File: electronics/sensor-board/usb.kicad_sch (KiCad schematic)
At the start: 6 parts, among them J16 USB_C_Receptacle_USB2.0

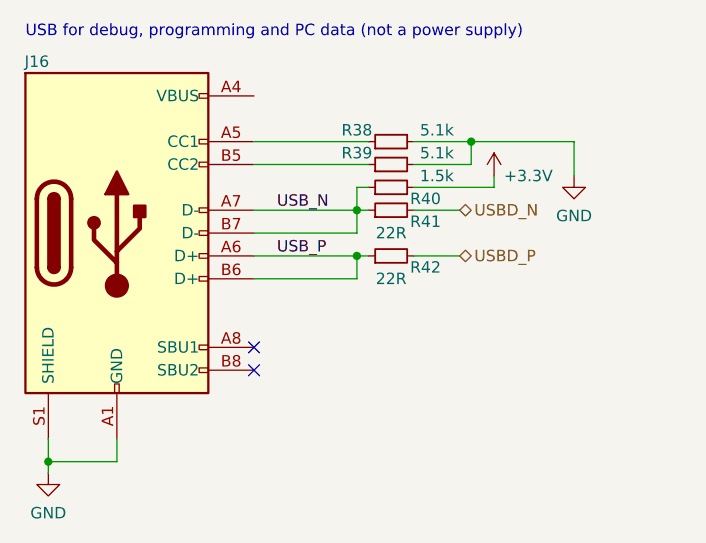
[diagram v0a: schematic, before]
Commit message: Upgrade to STM32G4 and CAN FD
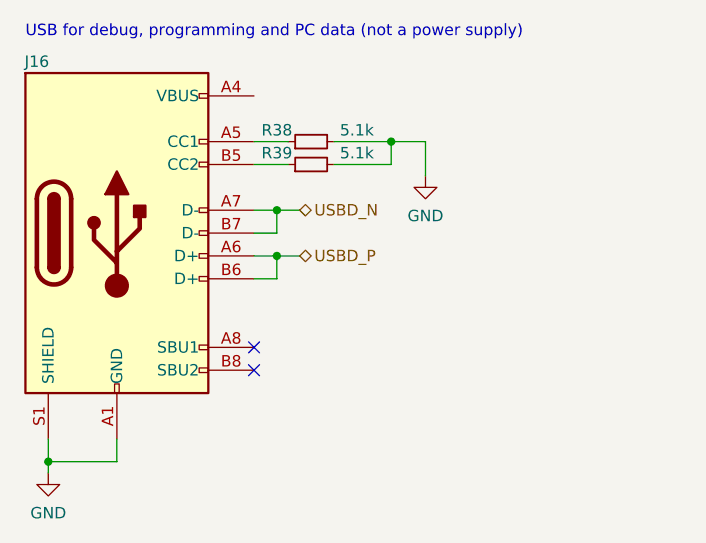
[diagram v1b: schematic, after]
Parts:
- removed R40: 1.5k, Resistor_SMD:R_0603_1608Metric, symbol Device:R_Small
- removed R41, R42: 22R, Resistor_SMD:R_0603_1608Metric, symbol Device:R_Small
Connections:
- net USB_N is gone; now on net USBD_N: J16.A7 (D-), J16.B7 (D-)
- net USB_P is gone; now on net USBD_P: J16.A6 (D+), J16.B6 (D+)
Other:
- moved on the sheet: R38, R39
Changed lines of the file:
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@@
 (kicad_sch (version 20211123) (generator eeschema)
   (paper "A4")
-  (junction (at 57.15 41.91) (diameter 0) (color 0 0 0 0)
+  (junction (at 48.26 41.91) (diameter 0) (color 0 0 0 0)
+  )
+  (junction (at 48.26 46.99) (diameter 0) (color 0 0 0 0)
   )
   (junction (at 22.86 69.85) (diameter 0) (color 0 0 0 0)
   )
-  (junction (at 69.85 34.29) (diameter 0) (color 0 0 0 0)
-  )
-  (junction (at 57.15 46.99) (diameter 0) (color 0 0 0 0)
+  (junction (at 60.96 34.29) (diameter 0) (color 0 0 0 0)
   )
   (no_connect (at 45.72 57.15))
@@
     (stroke (width 0) (type default) (color 0 0 0 0))
   )
-  (wire (pts (xy 69.85 34.29) (xy 81.28 34.29))
+  (wire (pts (xy 45.72 46.99) (xy 48.26 46.99))
     (stroke (width 0) (type default) (color 0 0 0 0))
   )
-  (wire (pts (xy 45.72 46.99) (xy 57.15 46.99))
+  (wire (pts (xy 45.72 36.83) (xy 49.53 36.83))
     (stroke (width 0) (type default) (color 0 0 0 0))
   )
-  (wire (pts (xy 45.72 36.83) (xy 58.42 36.83))
-    (stroke (width 0) (type default) (color 0 0 0 0))
-  )
-  (wire (pts (xy 45.72 41.91) (xy 57.15 41.91))
+  (wire (pts (xy 60.96 34.29) (xy 64.77 34.29))
     (stroke (width 0) (type default) (color 0 0 0 0))
   )
@@
     (stroke (width 0) (type default) (color 0 0 0 0))
   )
-  (wire (pts (xy 57.15 46.99) (xy 58.42 46.99))
-    (stroke (width 0) (type default) (color 0 0 0 0))
-  )
-  (wire (pts (xy 57.15 39.37) (xy 58.42 39.37))
-    (stroke (width 0) (type default) (color 0 0 0 0))
-  )
-  (wire (pts (xy 69.85 36.83) (xy 69.85 34.29))
+  (wire (pts (xy 60.96 36.83) (xy 60.96 34.29))
     (stroke (width 0) (type default) (color 0 0 0 0))
   )
@@
     (stroke (width 0) (type default) (color 0 0 0 0))
   )
-  (wire (pts (xy 63.5 39.37) (xy 72.39 39.37))
+  (wire (pts (xy 48.26 46.99) (xy 50.8 46.99))
     (stroke (width 0) (type default) (color 0 0 0 0))
   )
-  (wire (pts (xy 57.15 41.91) (xy 57.15 39.37))
+  (wire (pts (xy 48.26 41.91) (xy 50.8 41.91))
     (stroke (width 0) (type default) (color 0 0 0 0))
   )
-  (wire (pts (xy 57.15 41.91) (xy 58.42 41.91))
+  (wire (pts (xy 48.26 46.99) (xy 48.26 49.53))
     (stroke (width 0) (type default) (color 0 0 0 0))
   )
-  (wire (pts (xy 63.5 46.99) (xy 68.58 46.99))
+  (wire (pts (xy 45.72 34.29) (xy 49.53 34.29))
     (stroke (width 0) (type default) (color 0 0 0 0))
   )
-  (wire (pts (xy 57.15 46.99) (xy 57.15 49.53))
+  (wire (pts (xy 48.26 41.91) (xy 48.26 44.45))
     (stroke (width 0) (type default) (color 0 0 0 0))
   )
-  (wire (pts (xy 45.72 34.29) (xy 58.42 34.29))
-    (stroke (width 0) (type default) (color 0 0 0 0))
-  )
-  (wire (pts (xy 57.15 41.91) (xy 57.15 44.45))
-    (stroke (width 0) (type default) (color 0 0 0 0))
-  )
-  (wire (pts (xy 63.5 41.91) (xy 68.58 41.91))
+  (wire (pts (xy 45.72 41.91) (xy 48.26 41.91))
     (stroke (width 0) (type default) (color 0 0 0 0))
   )
@@
     (stroke (width 0) (type default) (color 0 0 0 0))
   )
-  (wire (pts (xy 69.85 34.29) (xy 63.5 34.29))
+  (wire (pts (xy 45.72 49.53) (xy 48.26 49.53))
     (stroke (width 0) (type default) (color 0 0 0 0))
   )
-  (wire (pts (xy 45.72 49.53) (xy 57.15 49.53))
+  (wire (pts (xy 54.61 36.83) (xy 60.96 36.83))
     (stroke (width 0) (type default) (color 0 0 0 0))
   )
-  (wire (pts (xy 63.5 36.83) (xy 69.85 36.83))
+  (wire (pts (xy 45.72 44.45) (xy 48.26 44.45))
     (stroke (width 0) (type default) (color 0 0 0 0))
   )
-  (wire (pts (xy 45.72 44.45) (xy 57.15 44.45))
+  (wire (pts (xy 64.77 34.29) (xy 64.77 38.1))
     (stroke (width 0) (type default) (color 0 0 0 0))
   )
-  (wire (pts (xy 81.28 34.29) (xy 81.28 38.1))
-    (stroke (width 0) (type default) (color 0 0 0 0))
-  )
-  (wire (pts (xy 72.39 39.37) (xy 72.39 38.1))
+  (wire (pts (xy 54.61 34.29) (xy 60.96 34.29))
     (stroke (width 0) (type default) (color 0 0 0 0))
   )
@@
     (effects (font (size 1.27 1.27)) (justify left bottom))
   )
-  (label "USB_P" (at 48.26 46.99 0)
-    (effects (font (size 1.27 1.27)) (justify left bottom))
-  )
-  (label "USB_N" (at 48.26 41.91 0)
-    (effects (font (size 1.27 1.27)) (justify left bottom))
-  )
-  (hierarchical_label "USBD_N" (shape bidirectional) (at 68.58 41.91 0)
+  (hierarchical_label "USBD_N" (shape bidirectional) (at 50.8 41.91 0)
     (effects (font (size 1.27 1.27)) (justify left))
   )
-  (hierarchical_label "USBD_P" (shape bidirectional) (at 68.58 46.99 0)
+  (hierarchical_label "USBD_P" (shape bidirectional) (at 50.8 46.99 0)
     (effects (font (size 1.27 1.27)) (justify left))
   )
-  (symbol (lib_id "power:GND") (at 81.28 38.1 0) (unit 1)
+  (symbol (lib_id "power:GND") (at 64.77 38.1 0) (unit 1)
     (in_bom yes) (on_board yes) (fields_autoplaced)
-    (property "Reference" "#PWR095" (id 0) (at 81.28 44.45 0)
+    (property "Reference" "#PWR095" (id 0) (at 64.77 44.45 0)
       (effects (font (size 1.27 1.27)) hide)
     )
-    (property "Value" "GND" (id 1) (at 81.28 42.5434 0))
-    (property "Footprint" "" (id 2) (at 81.28 38.1 0)
+    (property "Value" "GND" (id 1) (at 64.77 42.5434 0))
+    (property "Footprint" "" (id 2) (at 64.77 38.1 0)
       (effects (font (size 1.27 1.27)) hide)
     )
-    (property "Datasheet" "" (id 3) (at 81.28 38.1 0)
+    (property "Datasheet" "" (id 3) (at 64.77 38.1 0)
       (effects (font (size 1.27 1.27)) hide)
     )
     (pin "1")
   )
-  (symbol (lib_id "Device:R_Small") (at 60.96 39.37 90) (unit 1)
+  (symbol (lib_id "Device:R_Small") (at 52.07 36.83 90) (unit 1)
     (in_bom yes) (on_board yes)
-    (property "Reference" "R40" (id 0) (at 64.77 40.64 90))
-    (property "Value" "1.5k" (id 1) (at 66.04 38.1 90))
-    (property "Footprint" "Resistor_SMD:R_0603_1608Metric" (id 2) (at 60.96 39.37 0)
+    (property "Reference" "R39" (id 0) (at 48.26 35.56 90))
+    (property "Value" "5.1k" (id 1) (at 57.15 35.56 90))
+    (property "Footprint" "Resistor_SMD:R_0603_1608Metric" (id 2) (at 52.07 36.83 0)
       (effects (font (size 1.27 1.27)) hide)
     )
-    (property "Datasheet" "~" (id 3) (at 60.96 39.37 0)
+    (property "Datasheet" "~" (id 3) (at 52.07 36.83 0)
       (effects (font (size 1.27 1.27)) hide)
     )
     (pin "1")
     (pin "2")
-  )
-  (symbol (lib_id "Device:R_Small") (at 60.96 36.83 90) (unit 1)
-    (in_bom yes) (on_board yes)
-    (property "Reference" "R39" (id 0) (at 57.15 35.56 90))
-    (property "Value" "5.1k" (id 1) (at 66.04 35.56 90))
-    (property "Footprint" "Resistor_SMD:R_0603_1608Metric" (id 2) (at 60.96 36.83 0)
-      (effects (font (size 1.27 1.27)) hide)
-    )
-    (property "Datasheet" "~" (id 3) (at 60.96 36.83 0)
-      (effects (font (size 1.27 1.27)) hide)
-    )
-    (pin "1")
-    (pin "2")
-  )
-  (symbol (lib_id "power:+3.3V") (at 72.39 38.1 0) (unit 1)
-    (in_bom yes) (on_board yes)
-    (property "Reference" "#PWR094" (id 0) (at 72.39 41.91 0)
-      (effects (font (size 1.27 1.27)) hide)
-    )
-    (property "Value" "+3.3V" (id 1) (at 76.2 38.1 0))
-    (property "Footprint" "" (id 2) (at 72.39 38.1 0)
-      (effects (font (size 1.27 1.27)) hide)
-    )
-    (property "Datasheet" "" (id 3) (at 72.39 38.1 0)
-      (effects (font (size 1.27 1.27)) hide)
-    )
-    (pin "1")
   )
   (symbol (lib_id "Connector:USB_C_Receptacle_USB2.0") (at 30.48 44.45 0) (unit 1)
@@
     (pin "S1")
   )
-  (symbol (lib_id "Device:R_Small") (at 60.96 34.29 90) (unit 1)
+  (symbol (lib_id "Device:R_Small") (at 52.07 34.29 90) (unit 1)
     (in_bom yes) (on_board yes)
-    (property "Reference" "R38" (id 0) (at 57.15 33.02 90))
-    (property "Value" "5.1k" (id 1) (at 66.04 33.02 90))
-    (property "Footprint" "Resistor_SMD:R_0603_1608Metric" (id 2) (at 60.96 34.29 0)
+    (property "Reference" "R38" (id 0) (at 48.26 33.02 90))
+    (property "Value" "5.1k" (id 1) (at 57.15 33.02 90))
+    (property "Footprint" "Resistor_SMD:R_0603_1608Metric" (id 2) (at 52.07 34.29 0)
       (effects (font (size 1.27 1.27)) hide)
     )
-    (property "Datasheet" "~" (id 3) (at 60.96 34.29 0)
+    (property "Datasheet" "~" (id 3) (at 52.07 34.29 0)
       (effects (font (size 1.27 1.27)) hide)
     )
@@
     (pin "1")
   )
-  (symbol (lib_id "Device:R_Small") (at 60.96 46.99 90) (unit 1)
-    (in_bom yes) (on_board yes)
-    (property "Reference" "R42" (id 0) (at 64.77 48.26 90))
-    (property "Value" "22R" (id 1) (at 60.96 49.53 90))
-    (property "Footprint" "Resistor_SMD:R_0603_1608Metric" (id 2) (at 60.96 46.99 0)
-      (effects (font (size 1.27 1.27)) hide)
-    )
-    (property "Datasheet" "~" (id 3) (at 60.96 46.99 0)
-      (effects (font (size 1.27 1.27)) hide)
-    )
-    (pin "1")
-    (pin "2")
-  )
-  (symbol (lib_id "Device:R_Small") (at 60.96 41.91 90) (unit 1)
-    (in_bom yes) (on_board yes)
-    (property "Reference" "R41" (id 0) (at 64.77 43.18 90))
-    (property "Value" "22R" (id 1) (at 60.96 44.45 90))
-    (property "Footprint" "Resistor_SMD:R_0603_1608Metric" (id 2) (at 60.96 41.91 0)
-      (effects (font (size 1.27 1.27)) hide)
-    )
-    (property "Datasheet" "~" (id 3) (at 60.96 41.91 0)
-      (effects (font (size 1.27 1.27)) hide)
-    )
-    (pin "1")
-    (pin "2")
-  )
 )
